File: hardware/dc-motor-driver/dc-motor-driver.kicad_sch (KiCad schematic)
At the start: 13 parts, among them J1 MOT, J6 VCC, J7 IMODE, U1 DRV8874PWPR

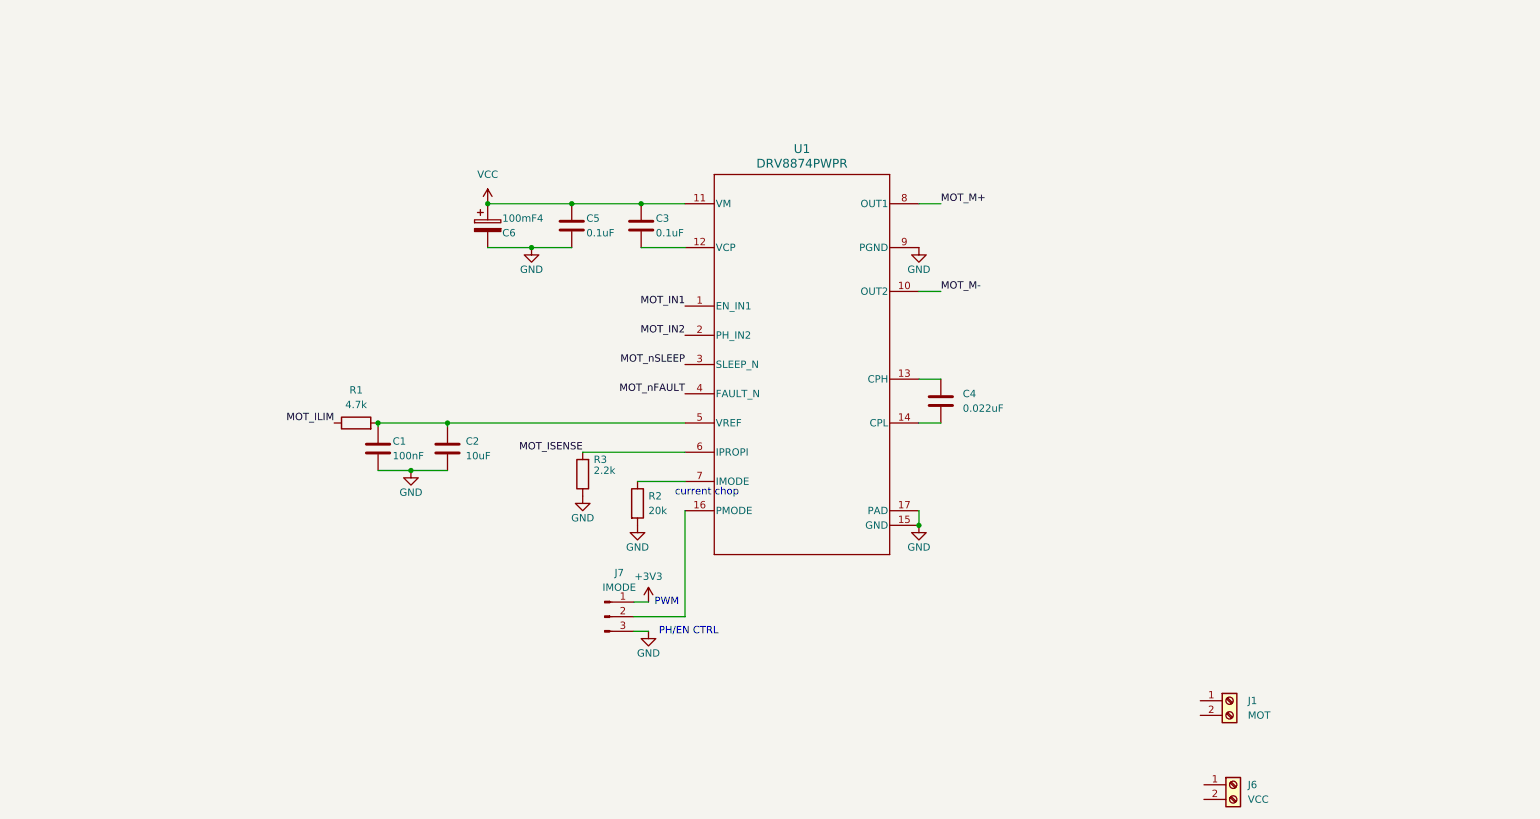
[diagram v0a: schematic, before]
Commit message: Footprints and BOM added
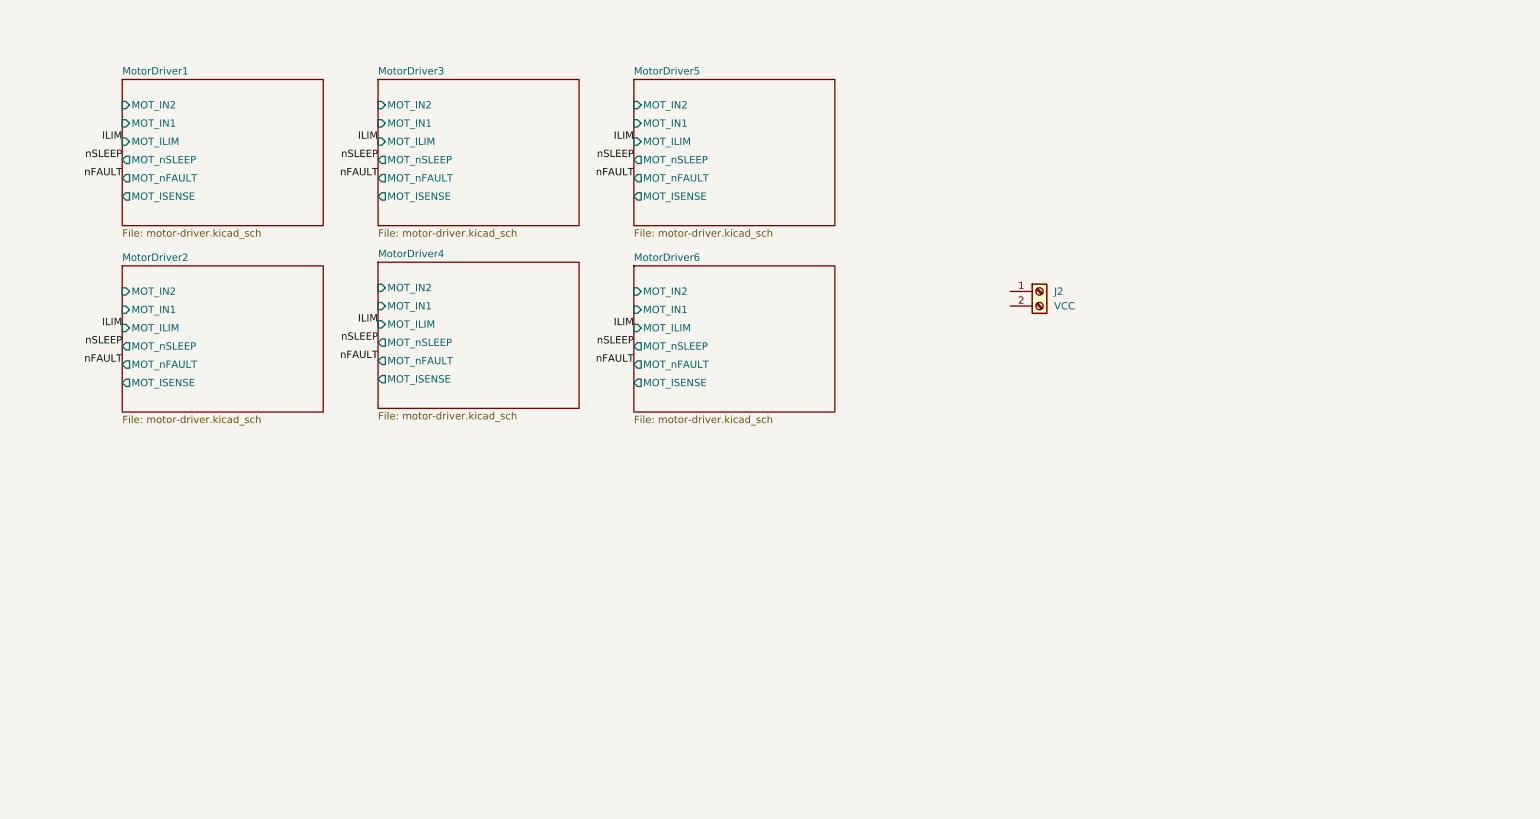
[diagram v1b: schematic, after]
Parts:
- removed 100mF4: C6, symbol Device:C_Polarized
- removed C1: 100nF, symbol Device:C
- removed C2: 10uF, symbol Device:C
- removed C3, C5: 0.1uF, symbol Device:C
- removed C4: 0.022uF, symbol Device:C
- removed J1: MOT, symbol Connector:Screw_Terminal_01x02
- removed J7: IMODE, symbol Connector:Conn_01x03_Pin
- removed R1: 4.7k, symbol Device:R
- removed R2: 20k, symbol Device:R
- removed R3: 2.2k, symbol Device:R
- removed U1: DRV8874PWPR, PWP0016J_N, symbol 2025-04-07_10-39-51:DRV8874PWPR
- J2: renamed from J6; footprint (none) -> TerminalBlock_4Ucon:TerminalBlock_4Ucon_1x02_P3.50mm_Horizontal
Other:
- added sheet MotorDriver1 (motor-driver.kicad_sch)
- added sheet MotorDriver2 (motor-driver.kicad_sch)
- added sheet MotorDriver3 (motor-driver.kicad_sch)
- added sheet MotorDriver4 (motor-driver.kicad_sch)
- added sheet MotorDriver5 (motor-driver.kicad_sch)
- added sheet MotorDriver6 (motor-driver.kicad_sch)
- note removed: "PH/EN CTRL"
- note removed: "PWM"
- note removed: "current chop"
- moved on the sheet: J2

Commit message: initial pcb routing
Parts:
- renumbered J2 to J1
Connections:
- net GND: now reaches J1.1 (Pin_1)
- net VCC: now reaches J1.2 (Pin_2)

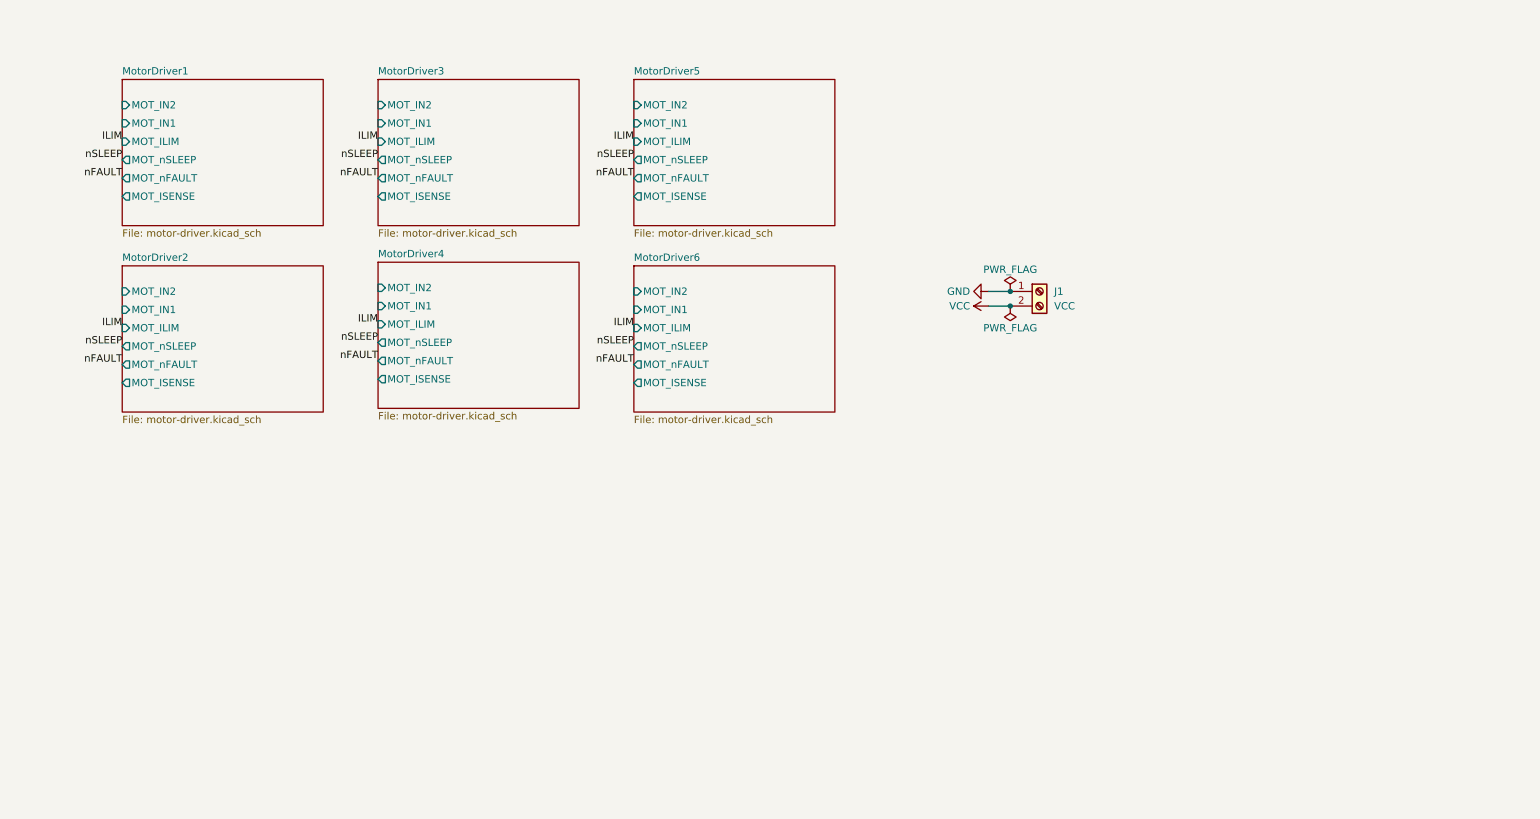
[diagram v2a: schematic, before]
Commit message: feat: WIP PCB layout
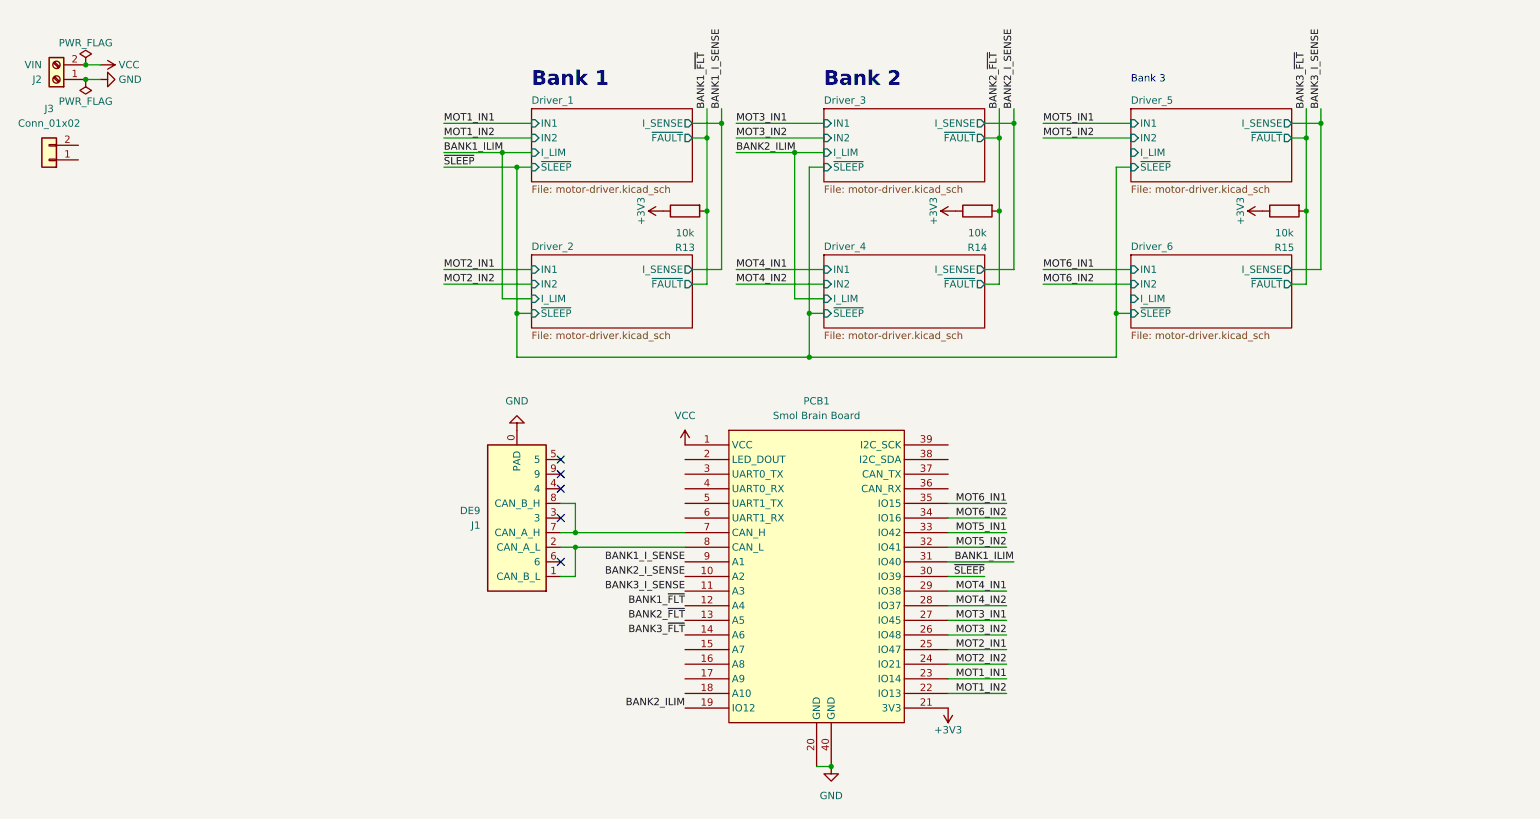
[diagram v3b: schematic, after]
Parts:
- added J1: DE9, THT:A-DF_09_A_KG-T2S, symbol Manufacturer_Connectors:A-DF_09_A/KG-T2S
- added J3: Conn_01x02, Connector_AMASS:AMASS_XT60PW-M_1x02_P7.20mm_Horizontal, symbol Connector_Generic:Conn_01x02
- added PCB1: Smol Brain Board, Project PCB:Smol_Brain_Board, symbol Project_PCB:Smol_Brain_Board
- added R13, R14, R15: 10k, Resistor_SMD:R_0603_1608Metric, symbol Resistor:R_10k_0603
- J2: renamed from J1; value VCC -> VIN
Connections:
- net GND: now also J1.0 (PAD), PCB1.20 (GND), PCB1.40 (GND)
- net VCC: now also PCB1.1 (VCC)
- new net: J1.7, J1.8, PCB1.7 (CAN_H)
- new net: J1.1, J1.2, PCB1.8 (CAN_L)
- new net +3V3: PCB1.21 (3V3), R13.2, R14.2, R15.2
- new net BANK1_ILIM: PCB1.31 (IO40)
- new net BANK1_I_SENSE: PCB1.9 (A1)
- new net BANK1_~{FLT}: PCB1.12 (A4), R13.1
- new net BANK2_ILIM: PCB1.19 (IO12)
- new net BANK2_I_SENSE: PCB1.10 (A2)
- new net BANK2_~{FLT}: PCB1.13 (A5), R14.1
- new net BANK3_I_SENSE: PCB1.11 (A3)
- new net BANK3_~{FLT}: PCB1.14 (A6), R15.1
- new net MOT1_IN1: PCB1.23 (IO14)
- new net MOT1_IN2: PCB1.22 (IO13)
- new net MOT2_IN1: PCB1.25 (IO47)
- new net MOT2_IN2: PCB1.24 (IO21)
- new net MOT3_IN1: PCB1.27 (IO45)
- new net MOT3_IN2: PCB1.26 (IO48)
- new net MOT4_IN1: PCB1.29 (IO38)
- new net MOT4_IN2: PCB1.28 (IO37)
- new net MOT5_IN1: PCB1.33 (IO42)
- new net MOT5_IN2: PCB1.32 (IO41)
- new net MOT6_IN1: PCB1.35 (IO15)
- new net MOT6_IN2: PCB1.34 (IO16)
- new net ~{SLEEP}: PCB1.30 (IO39)
- no-connect marks 0 -> 5
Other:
- sheet MotorDriver1 renamed Driver_1
- removed sheet MotorDriver2
- removed sheet MotorDriver3
- removed sheet MotorDriver4
- removed sheet MotorDriver5
- removed sheet MotorDriver6
- added sheet Driver_2 (motor-driver.kicad_sch)
- added sheet Driver_3 (motor-driver.kicad_sch)
- added sheet Driver_4 (motor-driver.kicad_sch)
- added sheet Driver_5 (motor-driver.kicad_sch)
- added sheet Driver_6 (motor-driver.kicad_sch)
- sheet Driver_1 ports: added IN1, IN2, I_LIM, I_SENSE, ~{FAULT}, ~{SLEEP}; removed MOT_ILIM, MOT_IN1, MOT_IN2, MOT_ISENSE, MOT_nFAULT, MOT_nSLEEP
- note added: "Bank 1"
- note added: "Bank 2"
- note added: "Bank 3"
- moved on the sheet: J2

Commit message: feat: DRC rules, more layout done
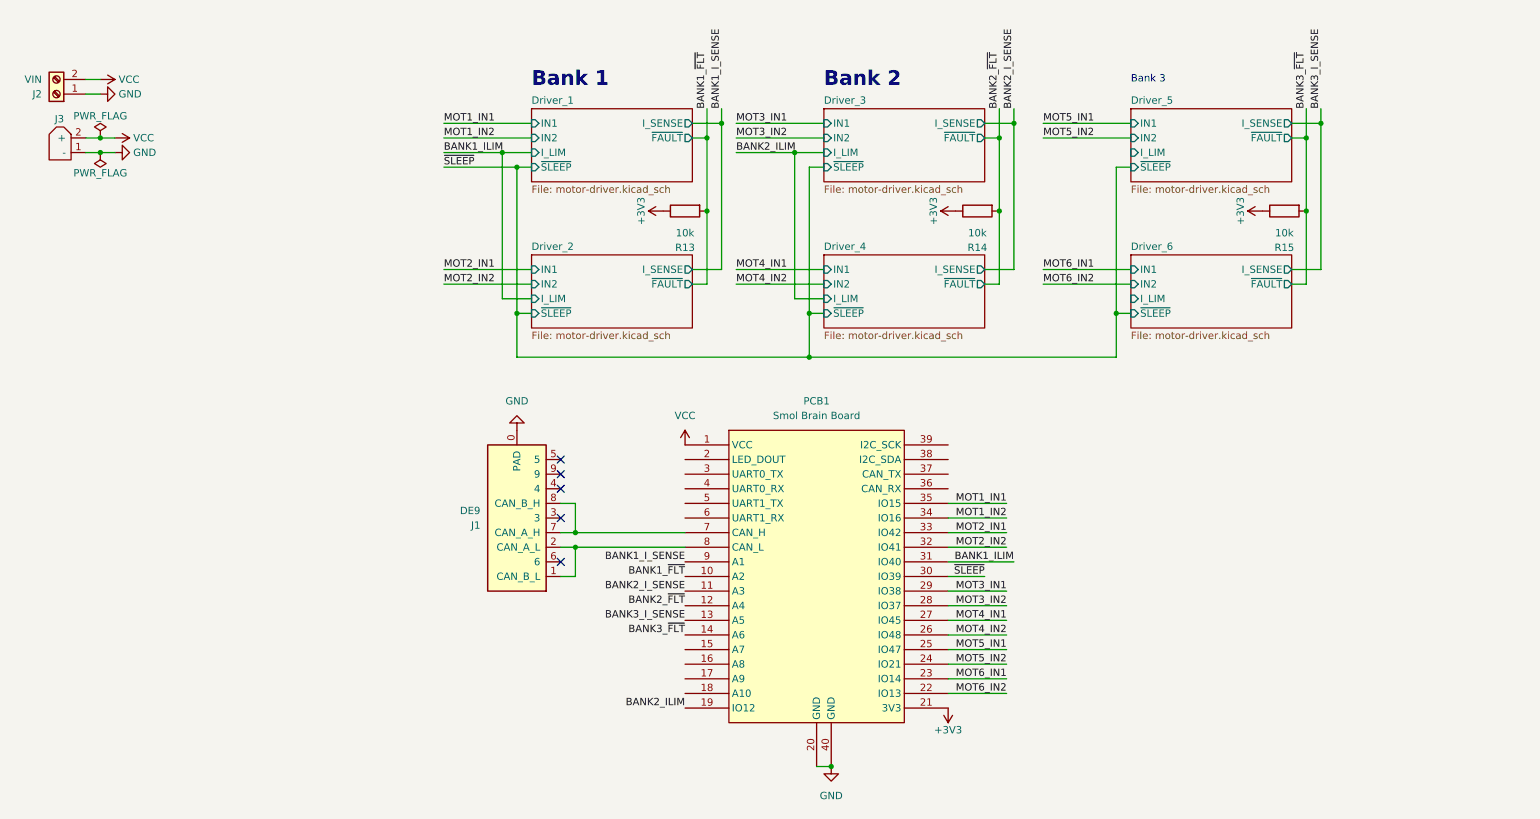
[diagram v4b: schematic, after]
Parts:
- removed J3: Conn_01x02, Connector_AMASS:AMASS_XT60PW-M_1x02_P7.20mm_Horizontal, symbol Connector_Generic:Conn_01x02
- added J3: ~, Connector_AMASS:AMASS_XT60PW-M_1x02_P7.20mm_Horizontal, symbol Manufacturer_Connectors:XT_Connector
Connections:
- net BANK1_~{FLT}: now also PCB1.10 (A2); no longer PCB1.12 (A4)
- net BANK2_I_SENSE: now also PCB1.11 (A3); no longer PCB1.10 (A2)
- net BANK2_~{FLT}: now also PCB1.12 (A4); no longer PCB1.13 (A5)
- net BANK3_I_SENSE: now also PCB1.13 (A5); no longer PCB1.11 (A3)
- net GND: now also J3.1 (-)
- net MOT1_IN1: now also PCB1.35 (IO15); no longer PCB1.23 (IO14)
- net MOT1_IN2: now also PCB1.34 (IO16); no longer PCB1.22 (IO13)
- net MOT2_IN1: now also PCB1.33 (IO42); no longer PCB1.25 (IO47)
- net MOT2_IN2: now also PCB1.32 (IO41); no longer PCB1.24 (IO21)
- net MOT3_IN1: now also PCB1.29 (IO38); no longer PCB1.27 (IO45)
- net MOT3_IN2: now also PCB1.28 (IO37); no longer PCB1.26 (IO48)
- net MOT4_IN1: now also PCB1.27 (IO45); no longer PCB1.29 (IO38)
- net MOT4_IN2: now also PCB1.26 (IO48); no longer PCB1.28 (IO37)
- net MOT5_IN1: now also PCB1.25 (IO47); no longer PCB1.33 (IO42)
- net MOT5_IN2: now also PCB1.24 (IO21); no longer PCB1.32 (IO41)
- net MOT6_IN1: now also PCB1.23 (IO14); no longer PCB1.35 (IO15)
- net MOT6_IN2: now also PCB1.22 (IO13); no longer PCB1.34 (IO16)
- net VCC: now also J3.2 (+)
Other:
- moved on the sheet: J2

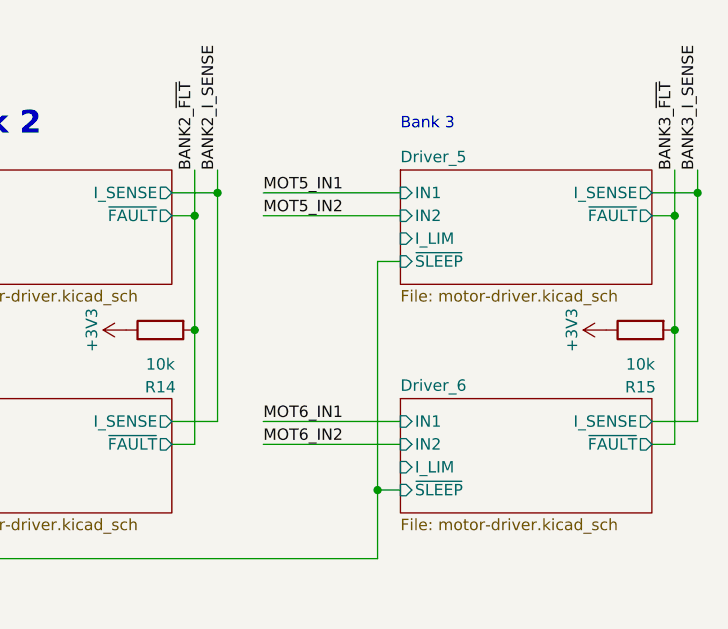
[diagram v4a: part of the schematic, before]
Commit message: Rough routing of motor_in for H-bridges
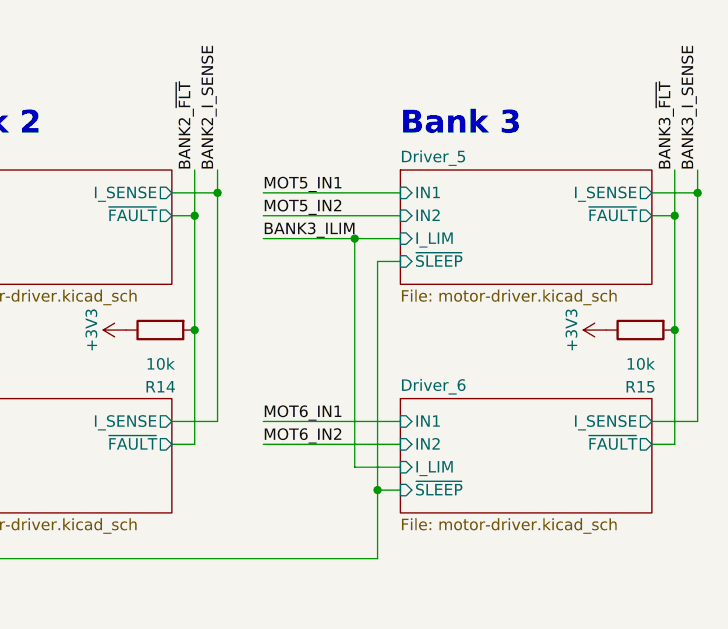
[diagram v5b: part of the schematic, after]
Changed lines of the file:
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@@
 	(generator_version "9.0")
 	(paper "A4")
-	(text "Bank 3"
-		(exclude_from_sim no)
-		(at 207.01 25.4 0)
-		(effects
-			(font
-				(size 1.27 1.27)
-			)
-			(justify left)
-		)
-	)
 	(text "Bank 2"
 		(exclude_from_sim no)
@@
 		)
 	)
+	(text "Bank 3\n"
+		(exclude_from_sim no)
+		(at 207.01 25.4 0)
+		(effects
+			(font
+				(size 2.54 2.54)
+				(thickness 0.508)
+				(bold yes)
+			)
+			(justify left)
+		)
+	)
 	(text "Bank 1"
 		(exclude_from_sim no)
@@
 	)
 	(junction
+		(at 201.93 38.1)
+		(diameter 0)
+		(color 0 0 0 0)
+	)
+	(junction
 		(at 100.33 40.64)
 		(diameter 0)
@@
 	(wire
 		(pts
+			(xy 201.93 38.1) (xy 207.01 38.1)
+		)
+		(stroke
+			(width 0)
+			(type default)
+		)
+	)
+	(wire
+		(pts
 			(xy 135.89 30.48) (xy 135.89 33.02)
 		)
@@
 	(wire
 		(pts
+			(xy 191.77 38.1) (xy 201.93 38.1)
+		)
+		(stroke
+			(width 0)
+			(type default)
+		)
+	)
+	(wire
+		(pts
 			(xy 191.77 33.02) (xy 207.01 33.02)
 		)
@@
 	(wire
 		(pts
+			(xy 207.01 63.5) (xy 201.93 63.5)
+		)
+		(stroke
+			(width 0)
+			(type default)
+		)
+	)
+	(wire
+		(pts
 			(xy 184.15 48.26) (xy 184.15 60.96)
+		)
+		(stroke
+			(width 0)
+			(type default)
+		)
+	)
+	(wire
+		(pts
+			(xy 201.93 63.5) (xy 201.93 38.1)
 		)
 		(stroke
@@
 		)
 	)
+	(label "BANK3_ILIM"
+		(at 191.77 38.1 0)
+		(effects
+			(font
+				(size 1.27 1.27)
+			)
+			(justify left bottom)
+		)
+	)

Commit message: feat: Routing progress
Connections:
- net BANK2_ILIM: now also PCB1.18 (A10); no longer PCB1.19 (IO12)
- net BANK3_ILIM: now also PCB1.19 (IO12)
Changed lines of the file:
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@@
+		)
+	)
+	(label "BANK3_ILIM"
+		(at 129.54 134.62 180)
+		(effects
+			(font
+				(size 1.27 1.27)
+			)
+			(justify right bottom)
 		)
 	)
@@
 	)
 	(label "BANK2_ILIM"
-		(at 129.54 134.62 180)
-		(effects
-			(font
+		(at 129.54 132.08 180)
+		(effects
+			(font
